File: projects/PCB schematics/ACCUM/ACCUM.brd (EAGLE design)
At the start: 43.2 x 64.4 mm, 14 parts, among them IC2 78L08SMD, Q2 IRLZ44Z

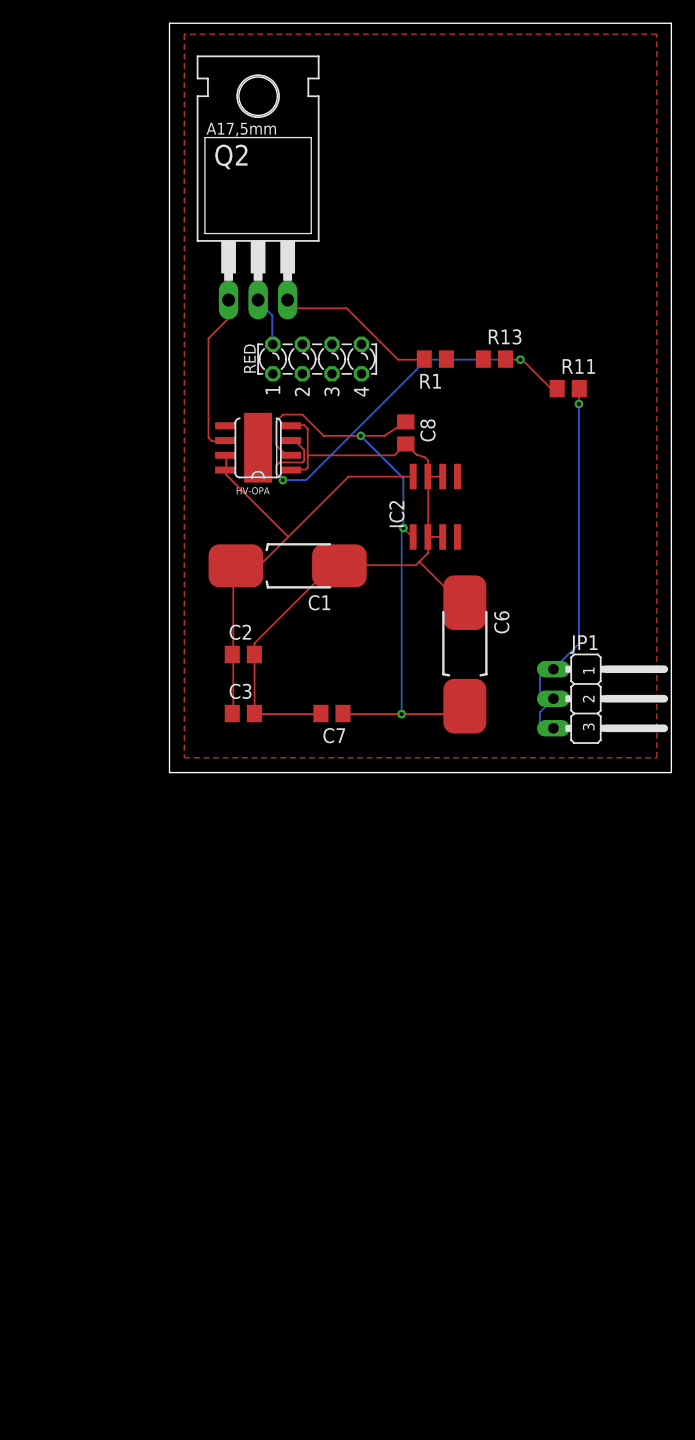
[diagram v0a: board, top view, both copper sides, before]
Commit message: ACCUM - Initial schematic revision.
Schematics have still not been properly updated from ESF versions.
In this commit, I've added in some external connectors (LED, etc.)

---SQUASH---

ACCUM - Initial revision; break to checkout TSALC.
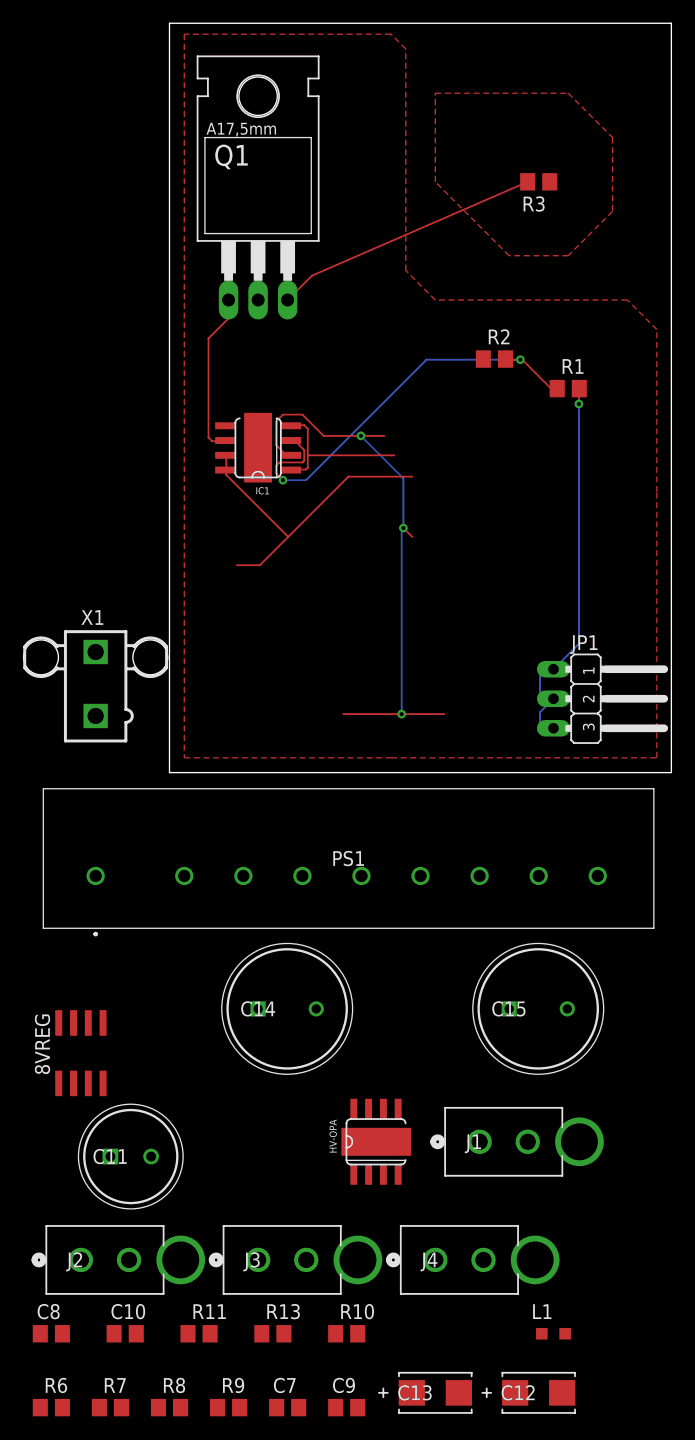
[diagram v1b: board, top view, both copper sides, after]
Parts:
- removed C1, C6: 10uF, rcl:085CS_1AW
- removed C2, C3: 0.1uF, rcl:C0805
- removed IC2: 78L08SMD, linear:SO08
- removed RED: LZR184, led:LZR184
- added 8VREG: L78L08ACD, linear:SO08
- added C10: 0.1uF, rcl:C0805
- added C11: EEU-FS1H221L, EEU-FS1H221L:CAPPRD350W65D800H2200
- added C12, C13: T491C106K020AT, T491C106K020AT:CAPT6032N
- added C14, C15: EKXF451ELL100MJ20S, EKXF451ELL100MJ20S:CAPPRD500W60D1025H2150
- added C9: 1uF, rcl:C0805
- added IC1: OPA454, OPA454:SO08GP
- added J1, J2, J3, J4: 2P_1-770166-0, con-MATE-N-LOK:CON2_1X2_P163_VMNL-1MTG
- added L1: 1mH, rcl:L2012C
- added PS1: M57184N-715B, M57184N-715B:M57184N715B
- added R10, R6, R7, R8, R9: 10k, rcl:R0805
- added R2: 100k, rcl:R0805
- added R3: (no value), rcl:R0805
- added X1: 5566-2, con-molex:5566-2
- C7: value 0.1uF -> 1uF
- R1: value (none) -> 680k
- R13: value 100k -> 120k
- moved R11 87.3 mm to (2.54, -48.3)
- moved R13 86.0 mm to (8.89, -48.3)
- moved C8 83.3 mm to (-10.2, -48.3), turned to 0 degrees
- moved HV-OPA 60.5 mm to (17.8, -31.8), turned to 0 degrees
- moved C7 59.8 mm to (10.2, -54.6), turned to 0 degrees
- moved R1 11.7 mm to (34.3, 33.0), turned to 0 degrees
- renumbered Q2 to Q1
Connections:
- removed net +12V: RED.A1
- new net +15V-NONISO: 8VREG.8, C11.1, C13.1, C7.1, C8.1, HV-OPA.7, HV-OPA.8, PS1.10
- new net ACCUM_LIGHT: Q1.D, X1.1, X1.2
- new net HV+: C14.1, J1.1, J1.2, PS1.1
- new net HV+_POST_AIR+: J2.1, J2.2, R11.2
- new net HV-_POST_AIR-: J3.1, J3.2, R13.1, R6.1
- new net N$1: L1.2, PS1.8
- new net N$3: C14.2, C15.1
- new net N$4: R7.2, R8.1
- new net N$5: R6.2, R7.1
- new net N$7: R8.2, R9.1
- new net N$8: R10.1, R9.2
- new net N$9: HV-OPA.6
- new net SIGNAL_VDIV: HV-OPA.3, R11.1, R13.2
- new net THERMAL: HV-OPA.THERMAL
- net +60V-POST-AIR_INDICATOR: now also IC1.6; no longer HV-OPA.6
- net +8V: now also 8VREG.1, C10.1, C12.1, C9.1, IC1.2; no longer C6.+, C7.1, C8.1, IC2.1
- net GND: now also R2.1, R3.1; no longer R1.1, R13.1
- net HV-: now also 8VREG.2, 8VREG.3, 8VREG.6, 8VREG.7, C10.2, C11.2, C12.2, C13.2, C15.2, C9.2, IC1.1, IC1.4, J4.1, J4.2, PS1.4, R10.2; no longer C1.-, C2.2, C3.2, C6.-, IC2.2, IC2.3, IC2.6, IC2.7
- net HV_POST_AIR: now also R1.2; no longer R11.2
- net N$2: now also L1.1, PS1.6; no longer Q1.D, RED.K1
- net N$6: now also R3.2; no longer R1.2
- net V+: now also IC1.7, IC1.8; no longer C1.+, C2.1, C3.1, HV-OPA.7, HV-OPA.8, IC2.8
- net VDIV_SIGNAL: now also IC1.3, R1.1, R2.2; no longer HV-OPA.3, R11.1, R13.2
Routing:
- net HV-: track 63.7 -> 13.9 mm
- net V+: track 40.6 -> 27.6 mm
- net N$6: track 13.9 -> 23.2 mm
- net N$2: track 4.34 -> 0.00 mm
- net +8V: track 53.5 -> 49.3 mm
- added copper zone on layer 1, net VCC
